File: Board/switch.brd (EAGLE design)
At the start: 50 x 50 mm, 31 parts, among them IC1 MCP2300X/SO, IC2 LM1117, U1 ADS1015

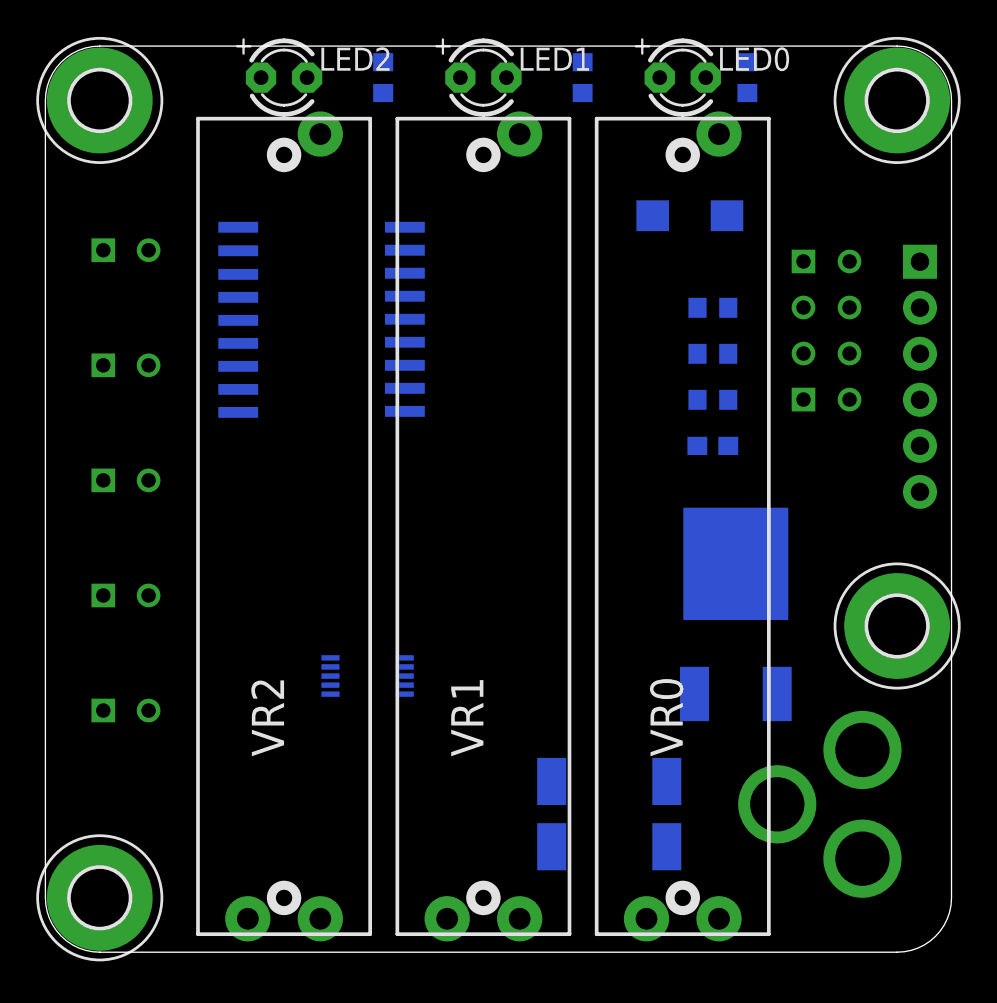
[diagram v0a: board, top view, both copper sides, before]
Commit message: Use PTA3043 footprint for slider
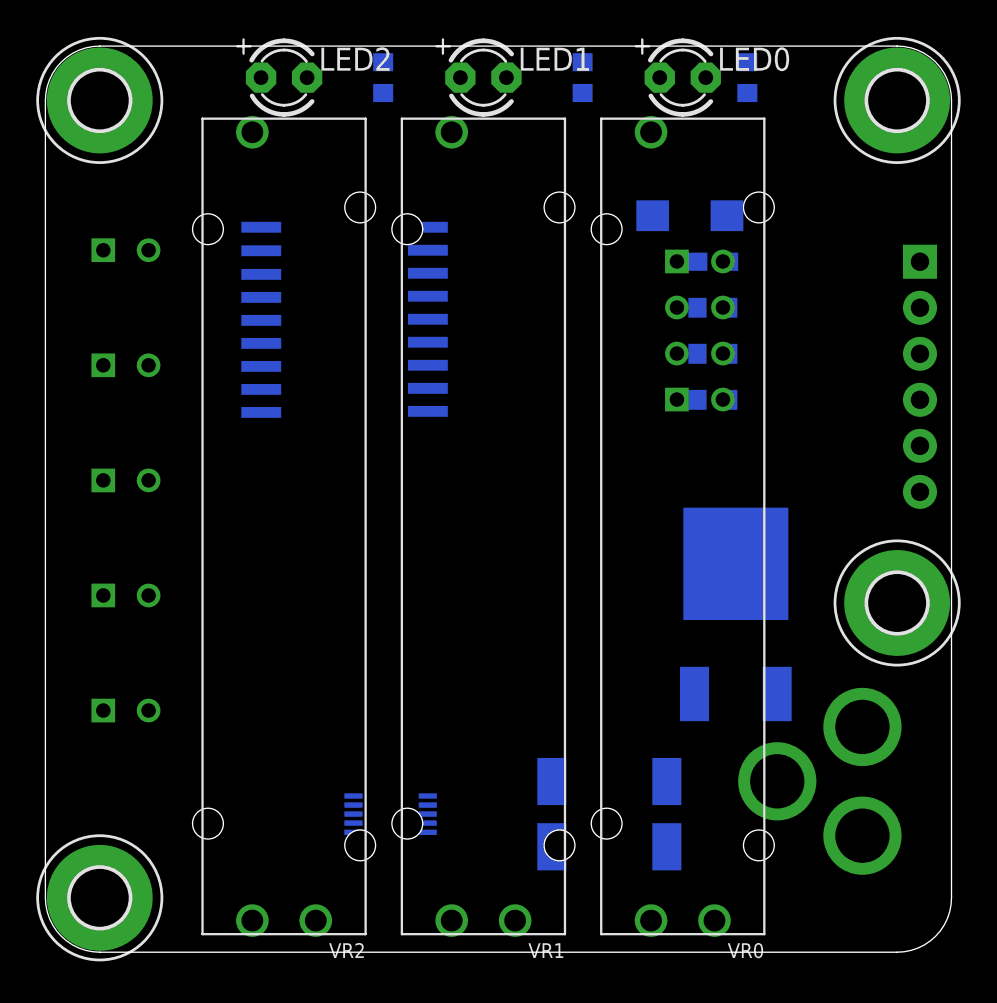
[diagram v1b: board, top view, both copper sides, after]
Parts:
- VR0, VR1, VR2: device SparkFun-Electromechanical:SLIDER-MEDIUM-KIT -> SparkFun-Electromechanical:PTA3043-2015CPB103
- moved C4 10.2 mm to (36.8, 38.1), turned to 0 degrees
- moved U1 7.73 mm to (19.1, 7.62)
- moved IC1 1.27 mm to (16.5, 35.6)
- moved DC-IN 1.27 mm to (45.1, -1.27)
- moved H1 1.27 mm to (47.0, 19.3)
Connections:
- net +3V3: now also VR0.P$3, VR1.P$3, VR2.P$3; no longer VR0.TOP, VR1.TOP, VR2.TOP
- net GND: now also VR0.P$1, VR1.P$1, VR2.P$1; no longer VR0.BOTTOM, VR1.BOTTOM, VR2.BOTTOM
- net N$3: now also VR2.P$2; no longer VR2.WIPER
- net N$4: now also VR1.P$2; no longer VR1.WIPER
- net N$5: now also VR0.P$2; no longer VR0.WIPER

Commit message: Use pcb-mount buttons
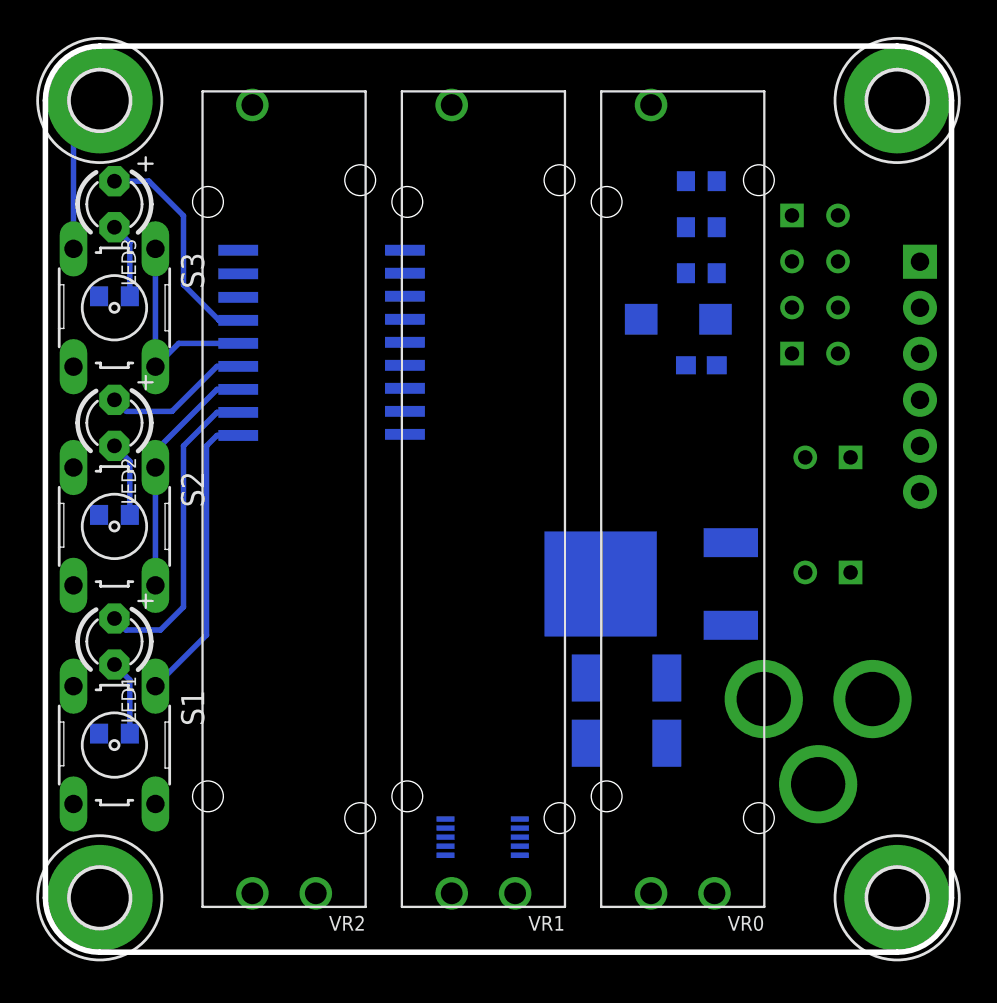
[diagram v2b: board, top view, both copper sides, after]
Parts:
- removed GP0, GP1, GP2: 02-JST, con-jst-xh:B2B-XH
- removed LED0: (no value), adafruit:LED3MM
- added LED3: (no value), adafruit:LED3MM
- added S1, S2, S3: (no value), switch-omron:B3F-10XX
- moved R5 50.3 mm to (3.81, 12.1), turned to 180 degrees
- moved GP4 42.6 mm to (43.2, 21.0), turned to 0 degrees
- moved GP3 39.1 mm to (43.2, 27.3), turned to 0 degrees
- moved LED1 37.2 mm to (3.81, 17.1), turned to 270 degrees
- moved R3 35.3 mm to (3.81, 24.1), turned to 180 degrees
- moved LED2 21.2 mm to (3.81, 29.2), turned to 270 degrees
- moved R2 19.1 mm to (3.81, 36.2), turned to 180 degrees
- moved DC-IN 17.3 mm to (53.3, 14.0), turned to 270 degrees
- moved H1 16.3 mm to (47.0, 3.00)
- moved R4 12.1 mm to (36.2, 42.5), turned to 0 degrees
- moved ESP-01 6.84 mm to (42.5, 36.8)
- moved C3 6.02 mm to (29.8, 13.3)
- moved D4 5.75 mm to (34.9, 34.9), turned to 180 degrees
- moved C4 5.75 mm to (36.2, 32.4)
- moved C2 5.72 mm to (34.3, 13.3)
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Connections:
- removed net DSD: GP2.P$1
- removed net N$11: IC1.6
- new net N$9: DC-IN.GND, DC-IN.GNDBREAK
- net +3V3: now also IC1.18, IC1.6
- net GND: now also S1.3, S1.4, S2.3, S2.4, S3.3, S3.4; no longer DC-IN.GND, DC-IN.GNDBREAK, GP0.P$1, GP1.P$1
- net GP0: now also S1.1; no longer GP0.P$2
- net GP1: now also LED1.A; no longer GP1.P$2
- net GP2: now also S2.1, S2.2; no longer GP2.P$2
- net GP3: now also LED2.A; no longer GP3.P$2
- net GP4: now also S3.1, S3.2; no longer GP4.P$2
- net GP5: now also LED3.A; no longer LED0.A
- net GP6: now also GP3.P$2; no longer LED1.A
- net GP7: now also GP4.P$2; no longer LED2.A
- net N$6: now also LED1.K; no longer LED0.K
- net N$7: now also LED2.K; no longer LED1.K
- net N$8: now also LED3.K; no longer LED2.K
- net VCC: no longer IC1.18
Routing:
- net GP1: track 0.00 -> 17.3 mm
- net GP0: track 0.00 -> 16.4 mm
- net GP2: track 0.00 -> 13.4 mm
- net GP5: track 0.00 -> 12.2 mm
- net GND: track 0.00 -> 12.0 mm
- net GP4: track 0.00 -> 11.6 mm
- net GP3: track 0.00 -> 7.22 mm
- net N$8: track 0.00 -> 4.16 mm
- net N$7: track 0.00 -> 4.16 mm
- net N$6: track 0.00 -> 4.16 mm

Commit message: Route traces and tweak layout
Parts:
- moved DC-IN 1.27 mm to (53.3, 12.7)
- turned LED1 to 90 degrees
- turned LED2 to 90 degrees
- turned LED3 to 90 degrees
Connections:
- removed net N$7: LED2.K, R3.2
- removed net N$9: DC-IN.GND, DC-IN.GNDBREAK
- new net N$10: LED3.A, R2.2
- net +3V3: now also R2.1, R3.1, R5.1
- net GND: now also DC-IN.GND, DC-IN.GNDBREAK; no longer R2.1, R3.1, R5.1
- net GP0: now also S1.2
- net GP1: now also LED1.K; no longer LED1.A
- net GP3: now also LED2.K; no longer LED2.A
- net GP5: now also LED3.K; no longer LED3.A
- net N$6: now also LED1.A; no longer LED1.K
- net N$8: now also LED2.A, R3.2; no longer LED3.K, R2.2
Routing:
- net GND: track 12.0 -> 279.2 mm, vias 0 -> 1
- net +3V3: track 0.00 -> 181.3 mm, vias 0 -> 4
- net I2C_SDA: track 0.00 -> 62.6 mm, vias 0 -> 2
- net I2C_SCL: track 0.00 -> 58.6 mm, vias 0 -> 2
- net GP7: track 0.00 -> 44.7 mm, vias 0 -> 1
- net GP6: track 0.00 -> 39.9 mm, vias 0 -> 1
- net N$2: track 0.00 -> 21.0 mm
- net N$5: track 0.00 -> 11.8 mm
- net VCC: track 0.00 -> 10.8 mm
- net N$1: track 0.00 -> 8.67 mm
- net RXI: track 0.00 -> 8.46 mm
- net N$3: track 0.00 -> 8.03 mm
- net RST: track 0.00 -> 8.01 mm
- net TXO: track 0.00 -> 6.97 mm
- net GP0: track 16.4 -> 23.1 mm
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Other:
- board text added: "Switch kleinpa.net REVA"
